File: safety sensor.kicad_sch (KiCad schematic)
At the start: 29 parts, among them IC1 STM8S003F3P6, J1 Conn_01x02, J2 Conn_01x01, J3 Conn_01x01, J4 Conn_01x01, J5 Conn_01x02, J6 Conn_01x01, U1 LD1117V33, U2 VCNL3020-GS08

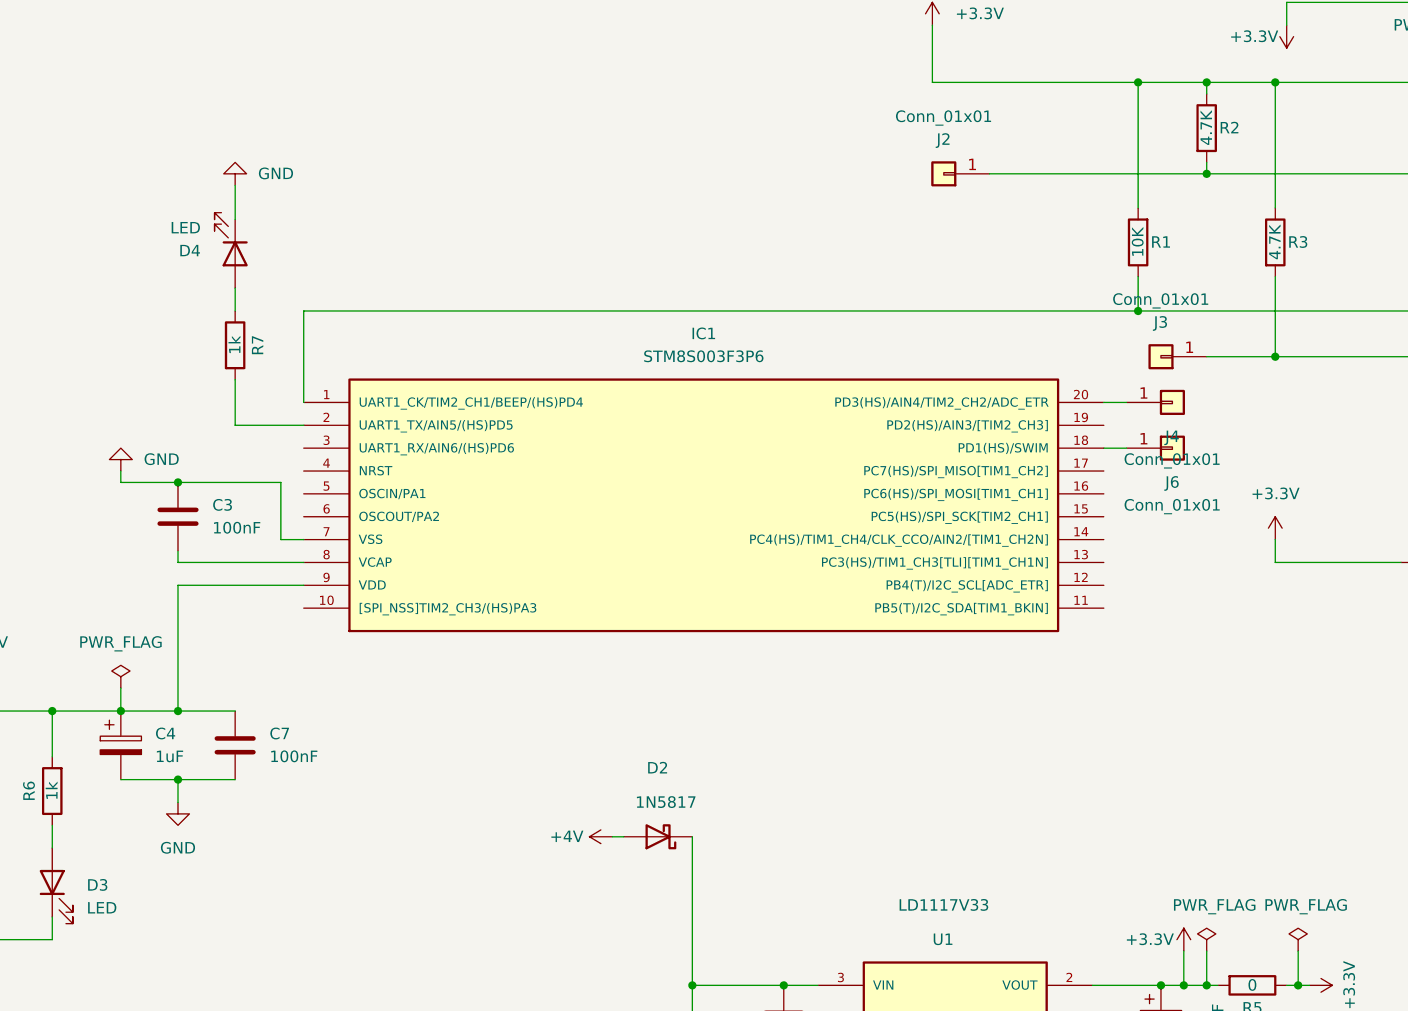
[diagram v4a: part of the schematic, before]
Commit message: flip stm8 chip, update from updated footrpint and connect it accordingly
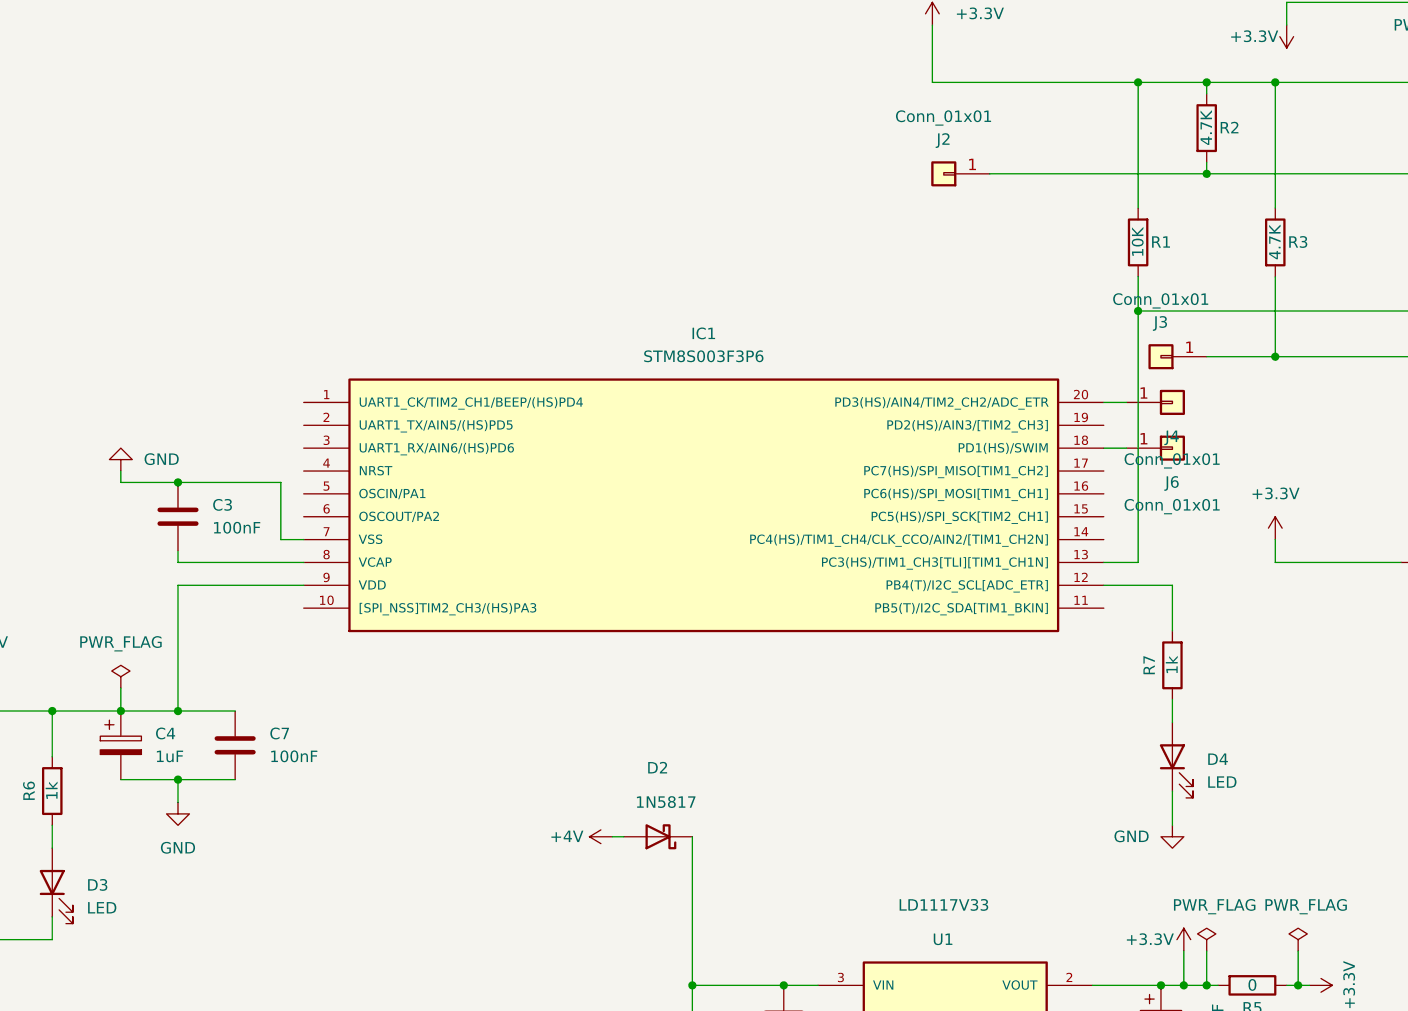
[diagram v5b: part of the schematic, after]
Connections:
- net at R7.2: now also IC1.12 (PB4(T)/I2C_SCL[ADC_ETR]); no longer IC1.2 (UART1_TX/AIN5/(HS)PD5)
- net at R1.1, U2.3: now also IC1.13 (PC3(HS)/TIM1_CH3[TLI][TIM1_CH1N]); no longer IC1.1 (UART1_CK/TIM2_CH1/BEEP/(HS)PD4)
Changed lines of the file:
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@@
-    (stroke (width 0) (type default) (color 0 0 0 0))
-  )
-  (wire (pts (xy 53.34 71.12) (xy 53.34 68.58))
     (stroke (width 0) (type default) (color 0 0 0 0))
   )
@@
     (stroke (width 0) (type default) (color 0 0 0 0))
   )
-  (wire (pts (xy 53.34 57.15) (xy 53.34 60.96))
+  (wire (pts (xy 157.48 114.3) (xy 157.48 116.84))
     (stroke (width 0) (type default) (color 0 0 0 0))
   )
@@
     (stroke (width 0) (type default) (color 0 0 0 0))
   )
+  (wire (pts (xy 153.67 71.12) (xy 153.67 99.06))
+    (stroke (width 0) (type default) (color 0 0 0 0))
+  )
   (wire (pts (xy 185.42 55.88) (xy 185.42 66.04))
     (stroke (width 0) (type default) (color 0 0 0 0))
@@
     (stroke (width 0) (type default) (color 0 0 0 0))
   )
-  (wire (pts (xy 53.34 83.82) (xy 60.96 83.82))
-    (stroke (width 0) (type default) (color 0 0 0 0))
-  )
   (wire (pts (xy 193.04 29.21) (xy 199.39 29.21))
     (stroke (width 0) (type default) (color 0 0 0 0))
@@
     (stroke (width 0) (type default) (color 0 0 0 0))
   )
-  (wire (pts (xy 60.96 81.28) (xy 60.96 71.12))
-    (stroke (width 0) (type default) (color 0 0 0 0))
-  )
   (wire (pts (xy 130.81 45.72) (xy 153.67 45.72))
     (stroke (width 0) (type default) (color 0 0 0 0))
@@
     (stroke (width 0) (type default) (color 0 0 0 0))
   )
-  (wire (pts (xy 60.96 71.12) (xy 153.67 71.12))
-    (stroke (width 0) (type default) (color 0 0 0 0))
-  )
-  (wire (pts (xy 53.34 78.74) (xy 53.34 83.82))
-    (stroke (width 0) (type default) (color 0 0 0 0))
-  )
   (wire (pts (xy 40.64 115.57) (xy 46.99 115.57))
     (stroke (width 0) (type default) (color 0 0 0 0))
@@
     (stroke (width 0) (type default) (color 0 0 0 0))
   )
+  (wire (pts (xy 157.48 128.27) (xy 157.48 124.46))
+    (stroke (width 0) (type default) (color 0 0 0 0))
+  )
+  (wire (pts (xy 149.86 99.06) (xy 153.67 99.06))
+    (stroke (width 0) (type default) (color 0 0 0 0))
+  )
   (wire (pts (xy 170.18 36.83) (xy 186.69 36.83))
     (stroke (width 0) (type default) (color 0 0 0 0))
@@
     (stroke (width 0) (type default) (color 0 0 0 0))
   )
+  (wire (pts (xy 157.48 101.6) (xy 149.86 101.6))
+    (stroke (width 0) (type default) (color 0 0 0 0))
+  )
   (wire (pts (xy 185.42 66.04) (xy 200.66 66.04))
+    (stroke (width 0) (type default) (color 0 0 0 0))
+  )
+  (wire (pts (xy 157.48 106.68) (xy 157.48 101.6))
     (stroke (width 0) (type default) (color 0 0 0 0))
   )
@@
     (pin "1")
   )
-  (symbol (lib_id "Device:R") (at 53.34 74.93 0) (unit 1)
-    (in_bom yes) (on_board yes)
-    (property "Reference" "R7" (id 0) (at 55.88 74.93 90))
-    (property "Value" "1k" (id 1) (at 53.34 74.93 90))
-    (property "Footprint" "Resistor_THT:R_Axial_DIN0207_L6.3mm_D2.5mm_P10.16mm_Horizontal" (id 2) (at 51.562 74.93 90)
-      (effects (font (size 1.27 1.27)) hide)
-    )
-    (property "Datasheet" "~" (id 3) (at 53.34 74.93 0)
+  (symbol (lib_id "Device:LED") (at 157.48 120.65 90) (unit 1)
+    (in_bom yes) (on_board yes) (fields_autoplaced)
+    (property "Reference" "D4" (id 0) (at 161.29 120.9674 90)
+      (effects (font (size 1.27 1.27)) (justify right))
+    )
+    (property "Value" "LED" (id 1) (at 161.29 123.5074 90)
+      (effects (font (size 1.27 1.27)) (justify right))
+    )
+    (property "Footprint" "LED_THT:LED_D5.0mm" (id 2) (at 157.48 120.65 0)
+      (effects (font (size 1.27 1.27)) hide)
+    )
+    (property "Datasheet" "~" (id 3) (at 157.48 120.65 0)
       (effects (font (size 1.27 1.27)) hide)
     )
@@
     )
     (pin "1")
-  )
-  (symbol (lib_id "Device:LED") (at 53.34 64.77 270) (unit 1)
-    (in_bom yes) (on_board yes) (fields_autoplaced)
-    (property "Reference" "D4" (id 0) (at 49.53 64.4526 90)
-      (effects (font (size 1.27 1.27)) (justify right))
-    )
-    (property "Value" "LED" (id 1) (at 49.53 61.9126 90)
-      (effects (font (size 1.27 1.27)) (justify right))
-    )
-    (property "Footprint" "LED_THT:LED_D5.0mm" (id 2) (at 53.34 64.77 0)
-      (effects (font (size 1.27 1.27)) hide)
-    )
-    (property "Datasheet" "~" (id 3) (at 53.34 64.77 0)
-      (effects (font (size 1.27 1.27)) hide)
-    )
-    (pin "1")
-    (pin "2")
   )
   (symbol (lib_id "power:GND") (at 201.93 109.22 0) (unit 1)
@@
     (pin "2")
   )
-  (symbol (lib_id "power:GND") (at 53.34 57.15 180) (unit 1)
-    (in_bom yes) (on_board yes) (fields_autoplaced)
-    (property "Reference" "#PWR0118" (id 0) (at 53.34 50.8 0)
-      (effects (font (size 1.27 1.27)) hide)
-    )
-    (property "Value" "GND" (id 1) (at 55.88 55.8799 0)
-      (effects (font (size 1.27 1.27)) (justify right))
-    )
-    (property "Footprint" "" (id 2) (at 53.34 57.15 0)
-      (effects (font (size 1.27 1.27)) hide)
-    )
-    (property "Datasheet" "" (id 3) (at 53.34 57.15 0)
-      (effects (font (size 1.27 1.27)) hide)
-    )
-    (pin "1")
-  )
   (symbol (lib_id "Device:C_Polarized") (at 156.21 149.86 0) (unit 1)
     (in_bom yes) (on_board yes)
@@
     (pin "1")
     (pin "2")
+  )
+  (symbol (lib_id "power:GND") (at 157.48 128.27 0) (unit 1)
+    (in_bom yes) (on_board yes) (fields_autoplaced)
+    (property "Reference" "#PWR0118" (id 0) (at 157.48 134.62 0)
+      (effects (font (size 1.27 1.27)) hide)
+    )
+    (property "Value" "GND" (id 1) (at 154.94 129.5401 0)
+      (effects (font (size 1.27 1.27)) (justify right))
+    )
+    (property "Footprint" "" (id 2) (at 157.48 128.27 0)
+      (effects (font (size 1.27 1.27)) hide)
+    )
+    (property "Datasheet" "" (id 3) (at 157.48 128.27 0)
+      (effects (font (size 1.27 1.27)) hide)
+    )
+    (pin "1")
   )
   (symbol (lib_id "Device:R") (at 33.02 124.46 180) (unit 1)
@@
     (pin "1")
   )
+  (symbol (lib_id "Device:R") (at 157.48 110.49 180) (unit 1)
+    (in_bom yes) (on_board yes)
+    (property "Reference" "R7" (id 0) (at 154.94 110.49 90))
+    (property "Value" "1k" (id 1) (at 157.48 110.49 90))
+    (property "Footprint" "Resistor_THT:R_Axial_DIN0207_L6.3mm_D2.5mm_P10.16mm_Horizontal" (id 2) (at 159.258 110.49 90)
+      (effects (font (size 1.27 1.27)) hide)
+    )
+    (property "Datasheet" "~" (id 3) (at 157.48 110.49 0)
+      (effects (font (size 1.27 1.27)) hide)
+    )
+    (pin "1")
+    (pin "2")
+  )
   (symbol (lib_id "power:PWR_FLAG") (at 171.45 142.24 0) (unit 1)
     (in_bom yes) (on_board yes)
@@
       (reference "#PWR0117") (unit 1) (value "+4V") (footprint "")
     )
-    (path "/4e04bf30-479f-4435-b94b-cdf5c6a1a382"
+    (path "/7997639c-d6b3-4967-bf66-d71db525babf"
       (reference "#PWR0118") (unit 1) (value "GND") (footprint "")
     )
@@
       (reference "D3") (unit 1) (value "LED") (footprint "LED_THT:LED_D5.0mm")
     )
-    (path "/2267d1ba-e829-4ba1-9443-8b81992ad025"
+    (path "/1c7882b5-7f41-46c5-865a-215e26b59025"
       (reference "D4") (unit 1) (value "LED") (footprint "LED_THT:LED_D5.0mm")
     )
@@
       (reference "R6") (unit 1) (value "1k") (footprint "Resistor_THT:R_Axial_DIN0207_L6.3mm_D2.5mm_P10.16mm_Horizontal")
     )
-    (path "/1de07f14-90f1-4949-be81-4d97191387b3"
+    (path "/e7f5e550-f264-4e87-aa56-0484c1e9d730"
       (reference "R7") (unit 1) (value "1k") (footprint "Resistor_THT:R_Axial_DIN0207_L6.3mm_D2.5mm_P10.16mm_Horizontal")
     )

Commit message: fixing track pad connection errors and polishing stm8 tssop20 footprint
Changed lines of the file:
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@@
+    (stroke (width 0) (type default) (color 0 0 0 0))
+  )
+  (wire (pts (xy 149.86 101.6) (xy 157.48 101.6))
     (stroke (width 0) (type default) (color 0 0 0 0))
   )
@@
     (stroke (width 0) (type default) (color 0 0 0 0))
   )
-  (wire (pts (xy 157.48 101.6) (xy 149.86 101.6))
-    (stroke (width 0) (type default) (color 0 0 0 0))
-  )

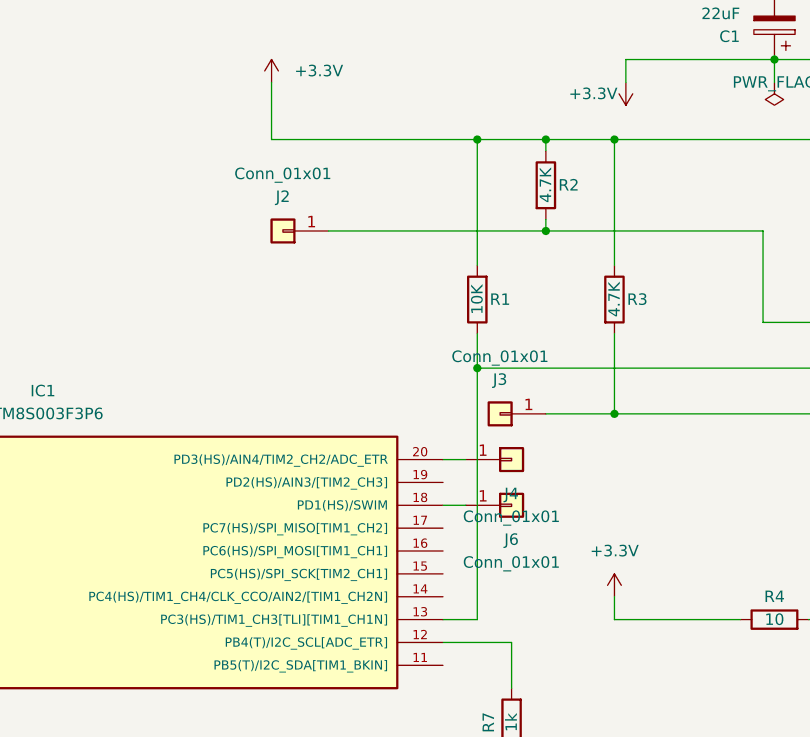
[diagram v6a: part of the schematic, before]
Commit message: pad name changes in schematic
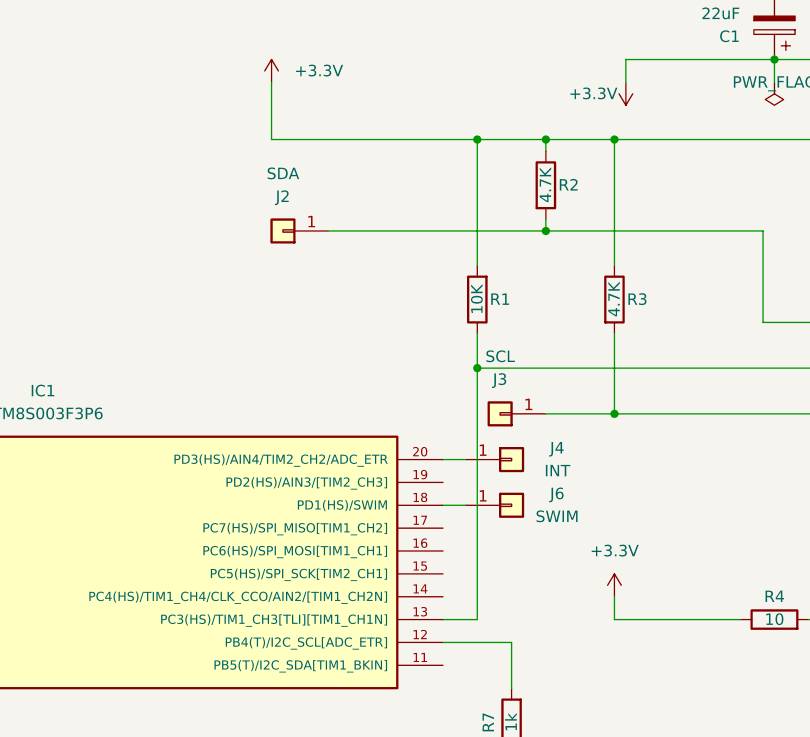
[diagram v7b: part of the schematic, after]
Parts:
- J2: value Conn_01x01 -> SDA
- J3: value Conn_01x01 -> SCL
- J4: value Conn_01x01 -> INT
- J6: value Conn_01x01 -> SWIM
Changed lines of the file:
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@@
   (symbol (lib_id "Connector_Generic:Conn_01x01") (at 157.48 81.28 0) (unit 1)
     (in_bom yes) (on_board yes)
-    (property "Reference" "J4" (id 0) (at 157.48 85.09 0))
-    (property "Value" "Conn_01x01" (id 1) (at 157.48 87.63 0))
+    (property "Reference" "J4" (id 0) (at 162.56 80.01 0))
+    (property "Value" "INT" (id 1) (at 162.56 82.55 0))
     (property "Footprint" "Connector_PinHeader_2.54mm:PinHeader_1x01_P2.54mm_Vertical" (id 2) (at 157.48 81.28 0)
       (effects (font (size 1.27 1.27)) hide)
@@
   (symbol (lib_id "Connector_Generic:Conn_01x01") (at 157.48 86.36 0) (unit 1)
     (in_bom yes) (on_board yes)
-    (property "Reference" "J6" (id 0) (at 157.48 90.17 0))
-    (property "Value" "Conn_01x01" (id 1) (at 157.48 92.71 0))
+    (property "Reference" "J6" (id 0) (at 162.56 85.09 0))
+    (property "Value" "SWIM" (id 1) (at 162.56 87.63 0))
     (property "Footprint" "Connector_PinHeader_2.54mm:PinHeader_1x01_P2.54mm_Vertical" (id 2) (at 157.48 86.36 0)
       (effects (font (size 1.27 1.27)) hide)
@@
     (in_bom yes) (on_board yes)
     (property "Reference" "J3" (id 0) (at 156.21 72.39 0))
-    (property "Value" "Conn_01x01" (id 1) (at 156.21 69.85 0))
+    (property "Value" "SCL" (id 1) (at 156.21 69.85 0))
     (property "Footprint" "Connector_PinHeader_2.54mm:PinHeader_1x01_P2.54mm_Vertical" (id 2) (at 156.21 76.2 0)
       (effects (font (size 1.27 1.27)) hide)
@@
     (in_bom yes) (on_board yes)
     (property "Reference" "J2" (id 0) (at 132.08 52.07 0))
-    (property "Value" "Conn_01x01" (id 1) (at 132.08 49.53 0))
+    (property "Value" "SDA" (id 1) (at 132.08 49.53 0))
     (property "Footprint" "Connector_PinHeader_2.54mm:PinHeader_1x01_P2.54mm_Vertical" (id 2) (at 132.08 55.88 0)
       (effects (font (size 1.27 1.27)) hide)
@@
     )
     (path "/ae23d2f4-6221-405a-b95d-a6a9d4d496f2"
-      (reference "J2") (unit 1) (value "Conn_01x01") (footprint "Connector_PinHeader_2.54mm:PinHeader_1x01_P2.54mm_Vertical")
+      (reference "J2") (unit 1) (value "SDA") (footprint "Connector_PinHeader_2.54mm:PinHeader_1x01_P2.54mm_Vertical")
     )
     (path "/96751c88-4b5f-46e7-91c1-ee9b489f2bcf"
-      (reference "J3") (unit 1) (value "Conn_01x01") (footprint "Connector_PinHeader_2.54mm:PinHeader_1x01_P2.54mm_Vertical")
+      (reference "J3") (unit 1) (value "SCL") (footprint "Connector_PinHeader_2.54mm:PinHeader_1x01_P2.54mm_Vertical")
     )
     (path "/5a1119dd-7d2f-4849-ac55-699475ecbfbf"
-      (reference "J4") (unit 1) (value "Conn_01x01") (footprint "Connector_PinHeader_2.54mm:PinHeader_1x01_P2.54mm_Vertical")
+      (reference "J4") (unit 1) (value "INT") (footprint "Connector_PinHeader_2.54mm:PinHeader_1x01_P2.54mm_Vertical")
     )
     (path "/9b2e425c-55fe-41d8-9c54-e65e6238c5c6"
@@
     )
     (path "/880751c1-2174-42b0-a015-b89b331b6e99"
-      (reference "J6") (unit 1) (value "Conn_01x01") (footprint "Connector_PinHeader_2.54mm:PinHeader_1x01_P2.54mm_Vertical")
+      (reference "J6") (unit 1) (value "SWIM") (footprint "Connector_PinHeader_2.54mm:PinHeader_1x01_P2.54mm_Vertical")
     )
     (path "/5f77b1fe-0a0b-49db-825a-edda5840d9b2"
